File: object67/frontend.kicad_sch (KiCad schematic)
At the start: 70 parts, among them IC4 TPA6120A2DWPR, J1 SN37A12B, U2 OPA1612AxD, U3 OPA1612AxD, U4 OPA1612AxD, U5 RCJ-2223, U6 OPA1612AxD

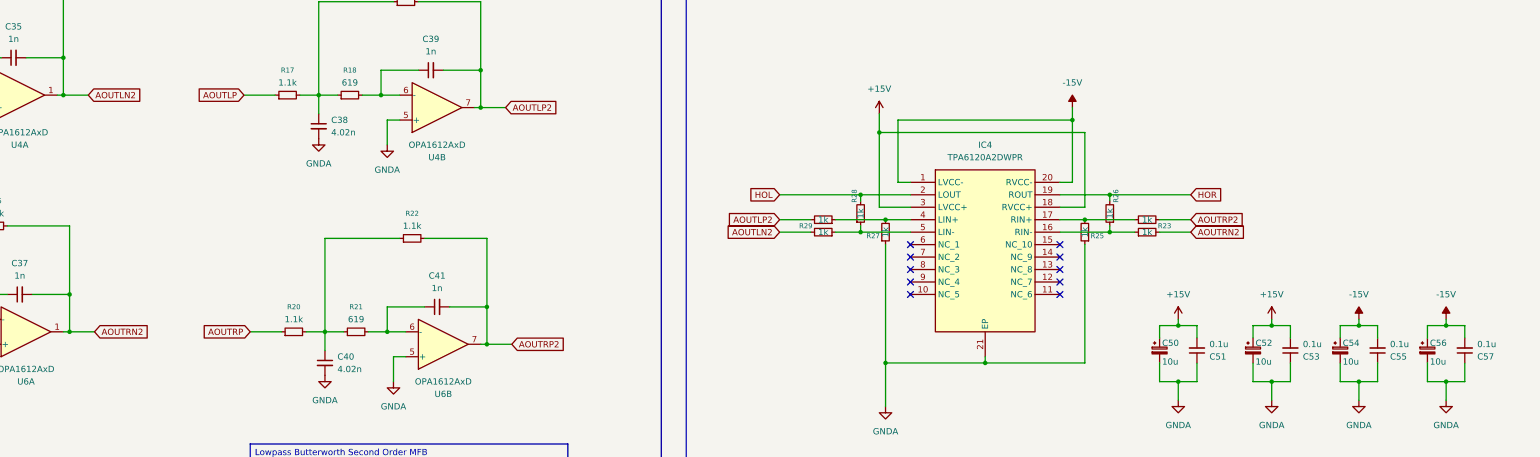
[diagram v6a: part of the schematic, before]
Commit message: Switching power supply
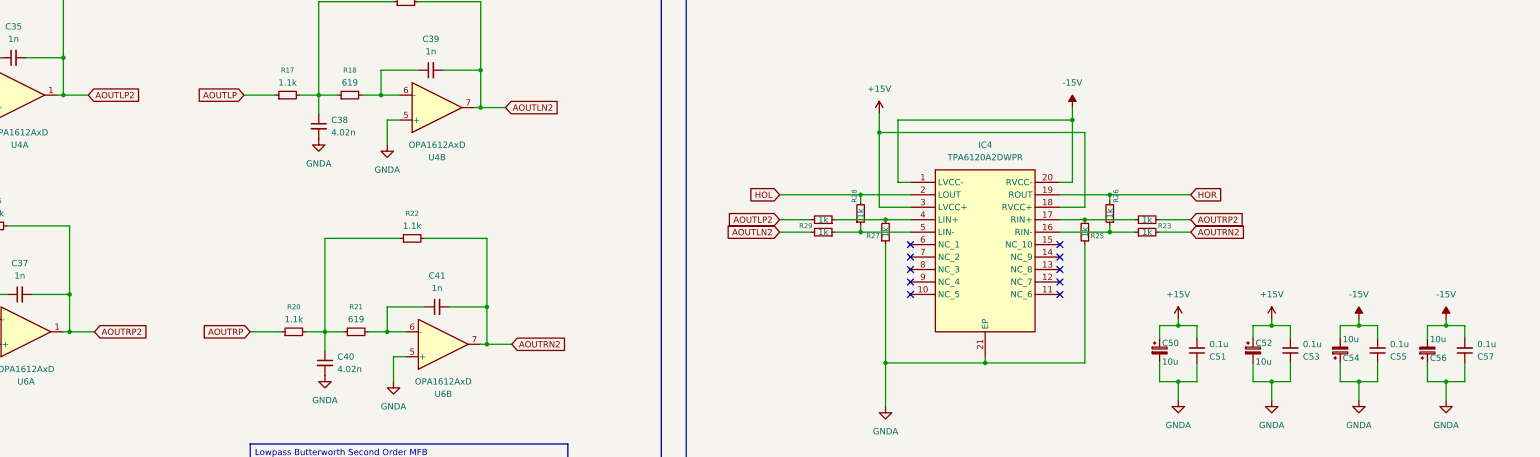
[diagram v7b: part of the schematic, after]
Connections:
- net -15V: now also C54.2, C56.2; no longer C54.1, C56.1
- net AOUTLN2: now also C39.2, R19.2, U4.7; no longer C35.2, R13.2, U4.1
- net AOUTLP2: now also C35.2, R13.2, U4.1; no longer C39.2, R19.2, U4.7
- net AOUTRN2: now also C41.2, R22.2, U6.7; no longer C37.2, R16.2, U6.1
- net AOUTRP2: now also C37.2, R16.2, U6.1; no longer C41.2, R22.2, U6.7
- net GNDA: now also C54.1, C56.1; no longer C54.2, C56.2
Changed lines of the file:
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@@
 		)
 	)
-	(global_label "AOUTRN2"
+	(global_label "AOUTRP2"
 		(shape input)
 		(at 88.9 185.42 0)
@@
 		)
 		(property "Intersheetrefs" "${INTERSHEET_REFS}"
-			(at 100.4124 185.42 0)
+			(at 100.3519 185.42 0)
 			(effects
 				(font
@@
 	(global_label "AOUTLP2"
 		(shape input)
-		(at 110.49 52.07 180)
+		(at 87.63 137.16 0)
 		(fields_autoplaced yes)
 		(effects
@@
 				(size 1.27 1.27)
 			)
-			(justify right)
+			(justify left)
 		)
 		(property "Intersheetrefs" "${INTERSHEET_REFS}"
-			(at 99.28 52.07 0)
+			(at 98.84 137.16 0)
 			(effects
 				(font
 					(size 1.27 1.27)
 				)
-				(justify right)
+				(justify left)
 				(hide yes)
 			)
 		)
 	)
-	(global_label "AOUTRN2"
+	(global_label "AOUTLP2"
 		(shape input)
-		(at 81.28 82.55 180)
+		(at 110.49 52.07 180)
 		(fields_autoplaced yes)
 		(effects
@@
 		)
 		(property "Intersheetrefs" "${INTERSHEET_REFS}"
-			(at 69.7676 82.55 0)
+			(at 99.28 52.07 0)
 			(effects
 				(font
@@
 		)
 	)
-	(global_label "AOUTLP2"
+	(global_label "AOUTRN2"
 		(shape input)
-		(at 228.6 162.56 180)
+		(at 81.28 82.55 180)
 		(fields_autoplaced yes)
 		(effects
@@
 		)
 		(property "Intersheetrefs" "${INTERSHEET_REFS}"
-			(at 217.39 162.56 0)
+			(at 69.7676 82.55 0)
 			(effects
 				(font
@@
 		)
 	)
-	(global_label "AOUTLN2"
+	(global_label "AOUTLP2"
 		(shape input)
-		(at 82.55 49.53 180)
+		(at 228.6 162.56 180)
 		(fields_autoplaced yes)
 		(effects
@@
 		)
 		(property "Intersheetrefs" "${INTERSHEET_REFS}"
-			(at 71.2795 49.53 0)
+			(at 217.39 162.56 0)
 			(effects
 				(font
@@
 		)
 	)
-	(global_label "HOR"
+	(global_label "AOUTLN2"
 		(shape input)
-		(at 113.03 248.92 0)
+		(at 82.55 49.53 180)
 		(fields_autoplaced yes)
 		(effects
@@
 				(size 1.27 1.27)
 			)
-			(justify left)
+			(justify right)
 		)
 		(property "Intersheetrefs" "${INTERSHEET_REFS}"
-			(at 119.9462 248.92 0)
+			(at 71.2795 49.53 0)
 			(effects
 				(font
 					(size 1.27 1.27)
 				)
-				(justify left)
+				(justify right)
 				(hide yes)
 			)
 		)
 	)
-	(global_label "AOUTLP2"
+	(global_label "HOR"
 		(shape input)
-		(at 172.72 139.7 0)
+		(at 113.03 248.92 0)
 		(fields_autoplaced yes)
 		(effects
@@
 		)
 		(property "Intersheetrefs" "${INTERSHEET_REFS}"
-			(at 183.93 139.7 0)
+			(at 119.9462 248.92 0)
 			(effects
 				(font
@@
 		)
 	)
-	(global_label "AOUTRP2"
+	(global_label "AOUTLN2"
 		(shape input)
-		(at 173.99 187.96 0)
+		(at 172.72 139.7 0)
 		(fields_autoplaced yes)
 		(effects
@@
 		)
 		(property "Intersheetrefs" "${INTERSHEET_REFS}"
-			(at 185.4419 187.96 0)
+			(at 183.9905 139.7 0)
 			(effects
 				(font
@@
 		)
 	)
-	(global_label "AOUTLN2"
+	(global_label "AOUTRN2"
 		(shape input)
-		(at 87.63 137.16 0)
+		(at 173.99 187.96 0)
 		(fields_autoplaced yes)
 		(effects
@@
 		)
 		(property "Intersheetrefs" "${INTERSHEET_REFS}"
-			(at 98.9005 137.16 0)
+			(at 185.5024 187.96 0)
 			(effects
 				(font
@@
 		(lib_id "Device:C_Polarized_Small")
 		(at 342.9 189.23 0)
+		(mirror x)
 		(unit 1)
 		(exclude_from_sim no)
@@
 		(dnp no)
 		(property "Reference" "C54"
-			(at 343.408 187.706 0)
+			(at 343.408 190.754 0)
 			(effects
 				(font
@@
 		)
 		(property "Value" "10u"
-			(at 343.408 191.516 0)
+			(at 343.408 186.944 0)
 			(effects
 				(font
@@
 		(lib_id "Device:C_Polarized_Small")
 		(at 360.68 189.23 0)
+		(mirror x)
 		(unit 1)
 		(exclude_from_sim no)
@@
 		(dnp no)
 		(property "Reference" "C56"
-			(at 361.188 187.706 0)
+			(at 361.188 190.754 0)
 			(effects
 				(font
@@
 		)
 		(property "Value" "10u"
-			(at 361.188 191.516 0)
+			(at 361.188 186.944 0)
 			(effects
 				(font

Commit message: Add LDO
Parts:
- added TP18, TP19, TP20, TP21, TP22, TP23: TestPoint, symbol Connector:TestPoint
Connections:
- net AOUTLN2: now also TP22.1
- net AOUTLP2: now also TP20.1
- net AOUTRN2: now also TP23.1
- net AOUTRP2: now also TP21.1
- net LL: now also TP18.1
- net LR: now also TP19.1
